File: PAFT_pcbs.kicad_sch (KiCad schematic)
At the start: 9 parts, among them U1 LM2596T-ADJ/LF02

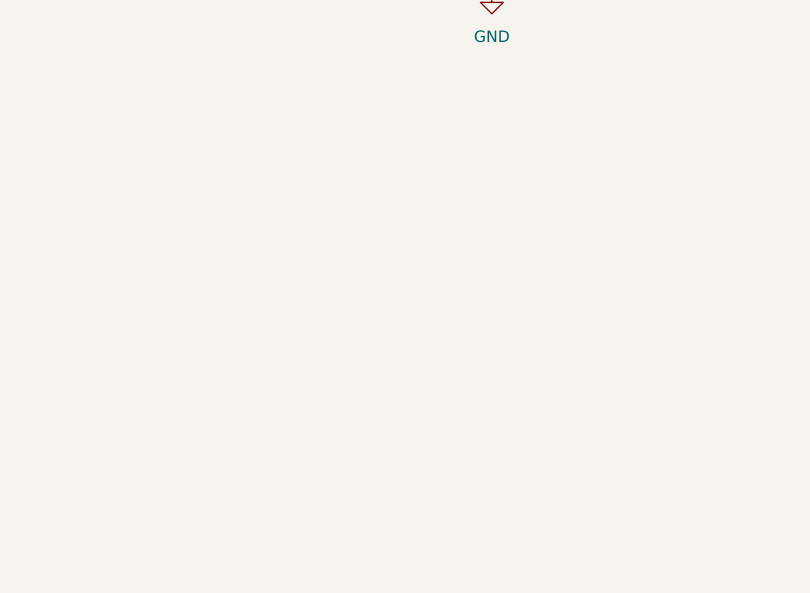
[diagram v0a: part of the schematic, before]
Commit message: added DRV8848
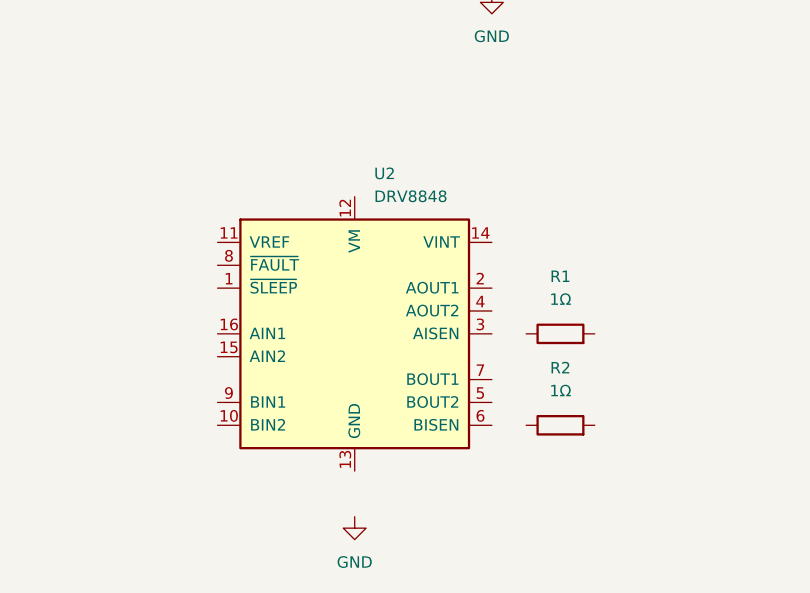
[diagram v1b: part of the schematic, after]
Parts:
- added R1, R2: 1Ω, symbol Device:R
- added U2: DRV8848, Package_SO:TSSOP-16-1EP_4.4x5mm_P0.65mm, symbol Driver_Motor:DRV8848
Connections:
- new net: U2.13 (GND), U2.17 (GND)

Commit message: add new sheets
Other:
- added sheet RPiUSBC (RPiUSBC.kicad_sch)
- added sheet ServoDriver (ServoDriver.kicad_sch)
- added sheet ServoPower (ServoPower.kicad_sch)
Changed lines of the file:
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@@
+		)
+	)
+	(sheet
+		(at 208.915 50.8)
+		(size 12.7 3.81)
+		(exclude_from_sim no)
+		(in_bom yes)
+		(on_board yes)
+		(dnp no)
+		(fields_autoplaced yes)
+		(stroke
+			(width 0.1524)
+			(type solid)
+		)
+		(fill
+			(color 0 0 0 0.0000)
+		)
+		(property "Sheetname" "ServoPower"
+			(at 208.915 50.0884 0)
+			(effects
+				(font
+					(size 1.27 1.27)
+				)
+				(justify left bottom)
+			)
+		)
+		(property "Sheetfile" "ServoPower.kicad_sch"
+			(at 208.915 55.1946 0)
+			(effects
+				(font
+					(size 1.27 1.27)
+				)
+				(justify left top)
+			)
+		)
+		(instances
+			(project "PAFT_pcbs"
+				(path "/8372e765-ead7-42d0-82da-59a3937ad504"
+					(page "3")
+				)
+			)
+		)
+	)
+	(sheet
+		(at 208.28 31.75)
+		(size 12.7 3.81)
+		(exclude_from_sim no)
+		(in_bom yes)
+		(on_board yes)
+		(dnp no)
+		(fields_autoplaced yes)
+		(stroke
+			(width 0.1524)
+			(type solid)
+		)
+		(fill
+			(color 0 0 0 0.0000)
+		)
+		(property "Sheetname" "ServoDriver"
+			(at 208.28 31.0384 0)
+			(effects
+				(font
+					(size 1.27 1.27)
+				)
+				(justify left bottom)
+			)
+		)
+		(property "Sheetfile" "ServoDriver.kicad_sch"
+			(at 208.28 36.1446 0)
+			(effects
+				(font
+					(size 1.27 1.27)
+				)
+				(justify left top)
+			)
+		)
+		(instances
+			(project "PAFT_pcbs"
+				(path "/8372e765-ead7-42d0-82da-59a3937ad504"
+					(page "2")
+				)
+			)
+		)
+	)
+	(sheet
+		(at 209.55 72.39)
+		(size 12.7 3.81)
+		(exclude_from_sim no)
+		(in_bom yes)
+		(on_board yes)
+		(dnp no)
+		(fields_autoplaced yes)
+		(stroke
+			(width 0.1524)
+			(type solid)
+		)
+		(fill
+			(color 0 0 0 0.0000)
+		)
+		(property "Sheetname" "RPiUSBC"
+			(at 209.55 71.6784 0)
+			(effects
+				(font
+					(size 1.27 1.27)
+				)
+				(justify left bottom)
+			)
+		)
+		(property "Sheetfile" "RPiUSBC.kicad_sch"
+			(at 209.55 76.7846 0)
+			(effects
+				(font
+					(size 1.27 1.27)
+				)
+				(justify left top)
+			)
+		)
+		(instances
+			(project "PAFT_pcbs"
+				(path "/8372e765-ead7-42d0-82da-59a3937ad504"
+					(page "4")
+				)
+			)
 		)
 	)

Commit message: update
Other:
- added sheet HBridge (HBridge.kicad_sch)
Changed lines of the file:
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@@
+		)
+	)
+	(sheet
+		(at 209.55 89.535)
+		(size 12.7 3.81)
+		(exclude_from_sim no)
+		(in_bom yes)
+		(on_board yes)
+		(dnp no)
+		(fields_autoplaced yes)
+		(stroke
+			(width 0.1524)
+			(type solid)
+		)
+		(fill
+			(color 0 0 0 0.0000)
+		)
+		(property "Sheetname" "HBridge"
+			(at 209.55 88.8234 0)
+			(effects
+				(font
+					(size 1.27 1.27)
+				)
+				(justify left bottom)
+			)
+		)
+		(property "Sheetfile" "HBridge.kicad_sch"
+			(at 209.55 93.9296 0)
+			(effects
+				(font
+					(size 1.27 1.27)
+				)
+				(justify left top)
+			)
+		)
+		(instances
+			(project "PAFT_pcbs"
+				(path "/8372e765-ead7-42d0-82da-59a3937ad504"
+					(page "5")
+				)
+			)
 		)
 	)

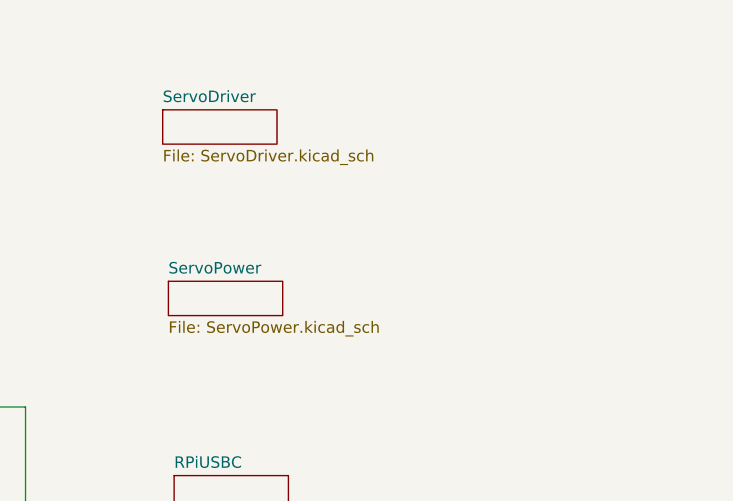
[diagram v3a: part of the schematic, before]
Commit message: ServoDriver schematic
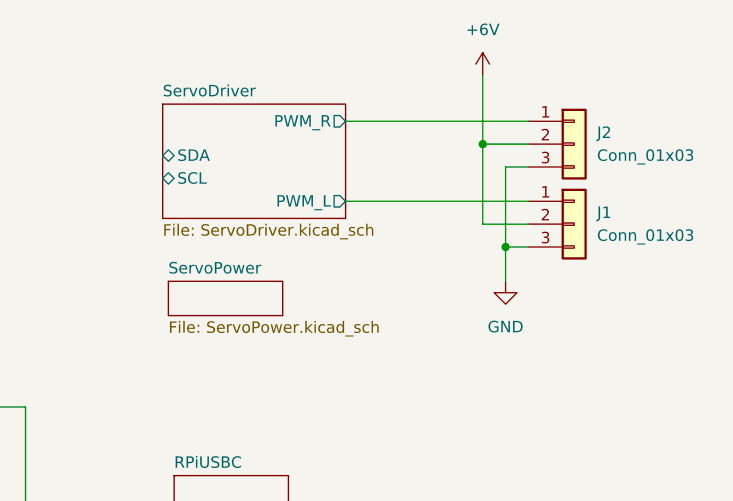
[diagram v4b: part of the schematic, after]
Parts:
- added J1, J2: Conn_01x03, symbol Connector_Generic:Conn_01x03
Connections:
- net GND: now also J1.3 (Pin_3), J2.3 (Pin_3)
- new net +6V: J1.2 (Pin_2), J2.2 (Pin_2)
- new net ServoDriver/PWM_L: J1.1 (Pin_1)
- new net ServoDriver/PWM_R: J2.1 (Pin_1)
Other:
- sheet ServoDriver ports: added PWM_L, PWM_R, SCL, SDA; removed none

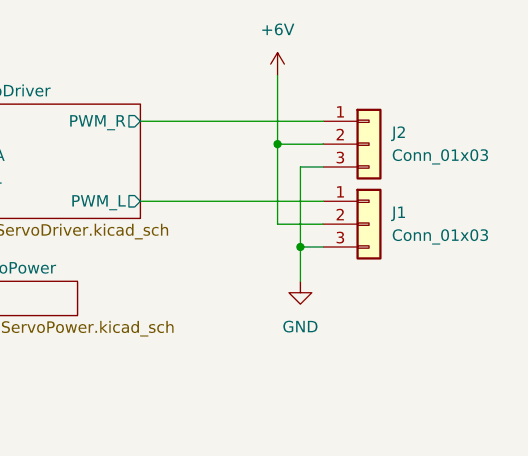
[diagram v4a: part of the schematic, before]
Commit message: HBridge top file connections (NOT CONNECTED TO TOP FILE YET)
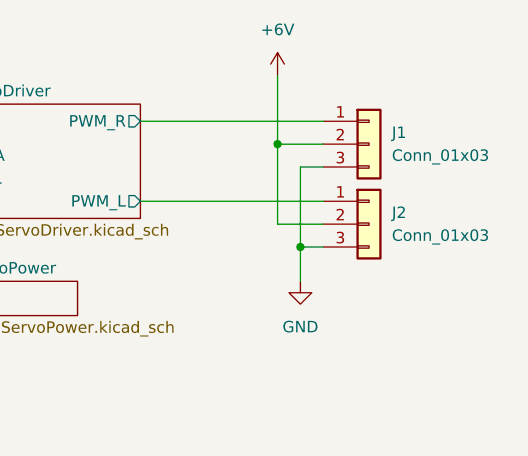
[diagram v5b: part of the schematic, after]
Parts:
- renumbered J2 to J1, J1 to J2
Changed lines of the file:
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@@
 		(dnp no)
 		(fields_autoplaced yes)
-		(property "Reference" "#PWR06"
+		(property "Reference" "#PWR05"
 			(at 246.38 57.15 0)
 			(effects
@@
 			(project ""
 				(path "/8372e765-ead7-42d0-82da-59a3937ad504"
-					(reference "#PWR06")
+					(reference "#PWR05")
 					(unit 1)
 				)
@@
 		(dnp no)
 		(fields_autoplaced yes)
-		(property "Reference" "#PWR07"
+		(property "Reference" "#PWR04"
 			(at 243.84 31.75 0)
 			(effects
@@
 			(project ""
 				(path "/8372e765-ead7-42d0-82da-59a3937ad504"
-					(reference "#PWR07")
+					(reference "#PWR04")
 					(unit 1)
 				)
@@
 		(dnp no)
 		(fields_autoplaced yes)
-		(property "Reference" "#PWR01"
+		(property "Reference" "#PWR02"
 			(at 116.84 125.73 0)
 			(effects
@@
 			(project ""
 				(path "/8372e765-ead7-42d0-82da-59a3937ad504"
-					(reference "#PWR01")
+					(reference "#PWR02")
 					(unit 1)
 				)
@@
 		(dnp no)
 		(fields_autoplaced yes)
-		(property "Reference" "#PWR03"
+		(property "Reference" "#PWR01"
 			(at 101.6 184.15 0)
 			(effects
@@
 			(project ""
 				(path "/8372e765-ead7-42d0-82da-59a3937ad504"
-					(reference "#PWR03")
+					(reference "#PWR01")
 					(unit 1)
 				)
@@
 		(dnp no)
 		(fields_autoplaced yes)
-		(property "Reference" "J2"
+		(property "Reference" "J1"
 			(at 256.54 34.2899 0)
 			(effects
@@
 			(project "PAFT_pcbs"
 				(path "/8372e765-ead7-42d0-82da-59a3937ad504"
-					(reference "J2")
+					(reference "J1")
 					(unit 1)
 				)
@@
 		(dnp no)
 		(fields_autoplaced yes)
-		(property "Reference" "#PWR02"
+		(property "Reference" "#PWR03"
 			(at 147.32 62.23 0)
 			(effects
@@
 			(project ""
 				(path "/8372e765-ead7-42d0-82da-59a3937ad504"
-					(reference "#PWR02")
+					(reference "#PWR03")
 					(unit 1)
 				)
@@
 		(dnp no)
 		(fields_autoplaced yes)
-		(property "Reference" "J1"
+		(property "Reference" "J2"
 			(at 256.54 43.1799 0)
 			(effects
@@
 			(project ""
 				(path "/8372e765-ead7-42d0-82da-59a3937ad504"
-					(reference "J1")
-					(unit 1)
-				)
+					(reference "J2")
+					(unit 1)
+				)

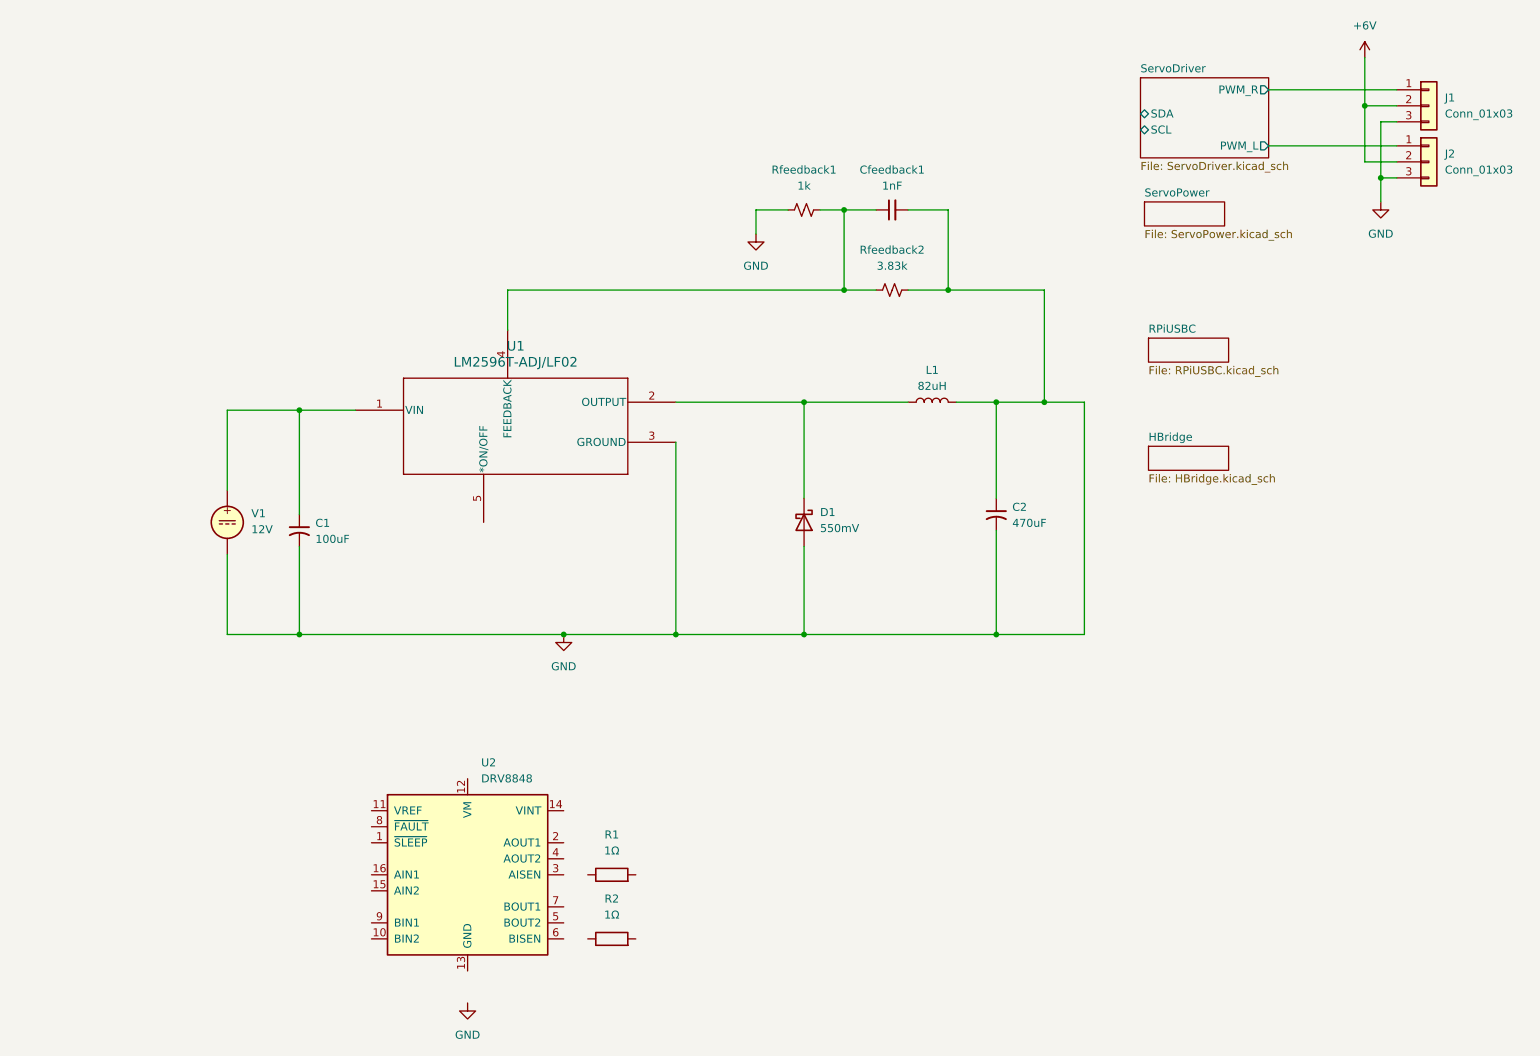
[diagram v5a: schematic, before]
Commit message: Servo Power added to child
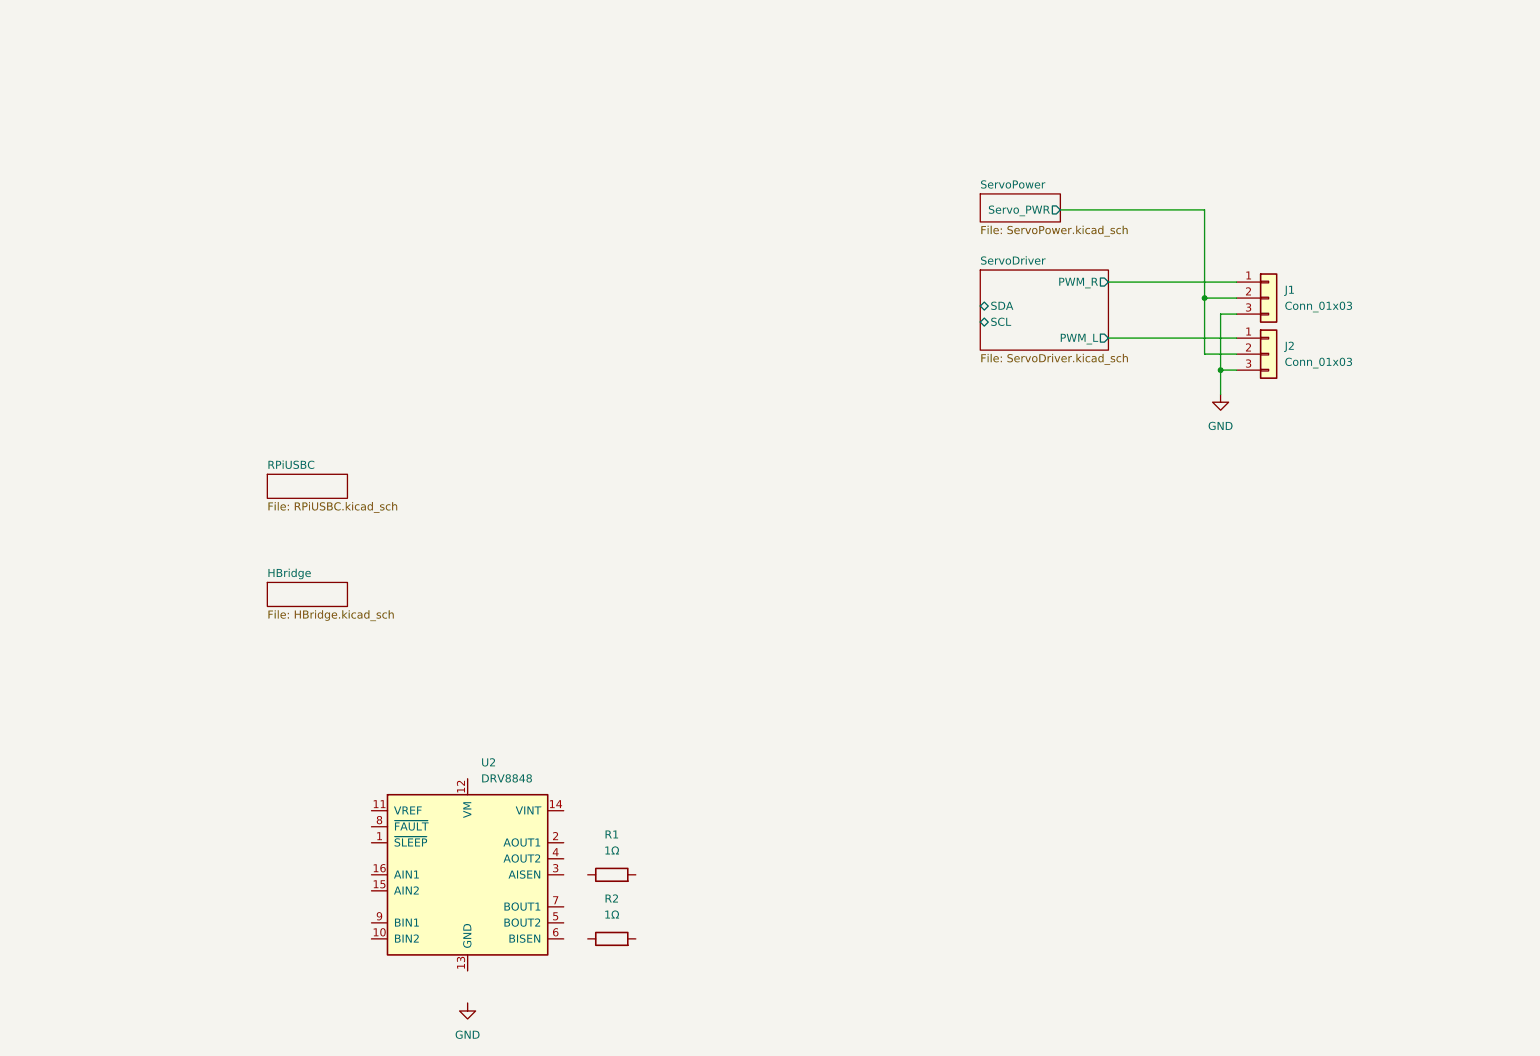
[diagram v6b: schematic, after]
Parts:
- removed C1: 100uF, symbol Device:C_Small_US
- removed C2: 470uF, symbol Device:C_Small_US
- removed Cfeedback1: 1nF, symbol Device:C_Small
- removed D1: 550mV, symbol Device:D_Schottky
- removed L1: 82uH, symbol Device:L
- removed Rfeedback1: 1k, symbol Device:R_Small_US
- removed Rfeedback2: 3.83k, symbol Device:R_Small_US
- removed U1: LM2596T-ADJ/LF02, NEB5_TEX, symbol 2026-01-27_05-04-46:LM2596T-ADJ_LF02
- removed V1: 12V, symbol Simulation_SPICE:VDC
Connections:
- net +6V renamed ServoPower/Servo_PWR
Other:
- sheet ServoPower ports: added Servo_PWR; removed none
- moved on the sheet: J1, J2

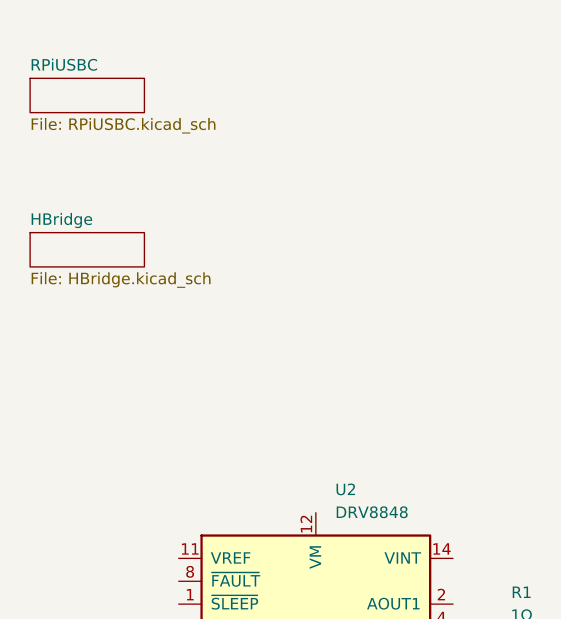
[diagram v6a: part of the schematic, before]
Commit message: Added HBridge pins to top schematic
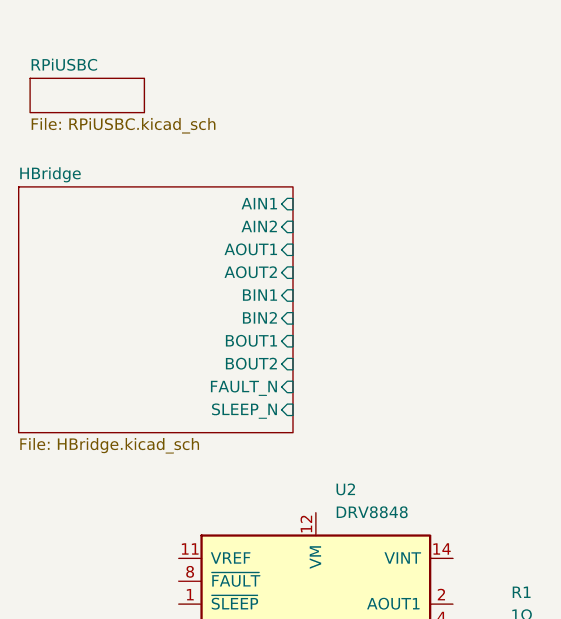
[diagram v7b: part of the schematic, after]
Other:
- sheet HBridge ports: added AIN1, AIN2, AOUT1, AOUT2, BIN1, BIN2, BOUT1, BOUT2, FAULT_N, SLEEP_N; removed none
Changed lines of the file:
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@@
 	)
 	(sheet
-		(at 69.85 111.125)
-		(size 12.7 3.81)
+		(at 68.58 106.045)
+		(size 30.48 27.305)
 		(exclude_from_sim no)
 		(in_bom yes)
@@
 		)
 		(property "Sheetname" "HBridge"
-			(at 69.85 110.4134 0)
+			(at 68.58 105.3334 0)
 			(effects
 				(font
@@
 		)
 		(property "Sheetfile" "HBridge.kicad_sch"
-			(at 69.85 115.5196 0)
+			(at 68.58 133.9346 0)
 			(effects
 				(font
@@
 			)
 		)
+		(pin "AIN1" input
+			(at 99.06 107.95 0)
+			(effects
+				(font
+					(size 1.27 1.27)
+				)
+				(justify right)
+			)
+		)
+		(pin "AIN2" input
+			(at 99.06 110.49 0)
+			(effects
+				(font
+					(size 1.27 1.27)
+				)
+				(justify right)
+			)
+		)
+		(pin "AOUT1" input
+			(at 99.06 113.03 0)
+			(effects
+				(font
+					(size 1.27 1.27)
+				)
+				(justify right)
+			)
+		)
+		(pin "AOUT2" input
+			(at 99.06 115.57 0)
+			(effects
+				(font
+					(size 1.27 1.27)
+				)
+				(justify right)
+			)
+		)
+		(pin "BIN1" input
+			(at 99.06 118.11 0)
+			(effects
+				(font
+					(size 1.27 1.27)
+				)
+				(justify right)
+			)
+		)
+		(pin "BIN2" input
+			(at 99.06 120.65 0)
+			(effects
+				(font
+					(size 1.27 1.27)
+				)
+				(justify right)
+			)
+		)
+		(pin "BOUT1" input
+			(at 99.06 123.19 0)
+			(effects
+				(font
+					(size 1.27 1.27)
+				)
+				(justify right)
+			)
+		)
+		(pin "BOUT2" input
+			(at 99.06 125.73 0)
+			(effects
+				(font
+					(size 1.27 1.27)
+				)
+				(justify right)
+			)
+		)
+		(pin "FAULT_N" input
+			(at 99.06 128.27 0)
+			(effects
+				(font
+					(size 1.27 1.27)
+				)
+				(justify right)
+			)
+		)
+		(pin "SLEEP_N" input
+			(at 99.06 130.81 0)
+			(effects
+				(font
+					(size 1.27 1.27)
+				)
+				(justify right)
+			)
+		)
